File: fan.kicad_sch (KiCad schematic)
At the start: 16 parts, among them J10 Conn_01x04, J16 Conn_02x03_Counter_Clockwise, J2 Conn_01x02, J7 Conn_01x04, J8 Conn_01x02, J9 Conn_01x04, Q1 SS8050, U2 ICM-20948, U3 TXS0104EPW, U7 MAX98357A

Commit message: feat: semi-finalized PCB design
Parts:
- H1, H2, H3, H4: footprint MountingHole:MountingHole_2.2mm_M2 -> MountingHole:MountingHole_3.2mm_M3
- J16: footprint (none) -> Connector_PinHeader_2.54mm:PinHeader_2x03_P2.54mm_Vertical
- J8: footprint (none) -> Connector_PinHeader_2.54mm:PinHeader_1x02_P2.54mm_Vertical
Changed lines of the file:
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@@
 			)
 		)
-		(property "Footprint" ""
+		(property "Footprint" "Connector_PinHeader_2.54mm:PinHeader_2x03_P2.54mm_Vertical"
 			(at 101.6 175.26 0)
 			(effects
@@
 			)
 		)
-		(property "Footprint" "MountingHole:MountingHole_2.2mm_M2"
+		(property "Footprint" "MountingHole:MountingHole_3.2mm_M3"
 			(at 147.32 110.49 0)
 			(effects
@@
 			)
 		)
-		(property "Footprint" "MountingHole:MountingHole_2.2mm_M2"
+		(property "Footprint" "MountingHole:MountingHole_3.2mm_M3"
 			(at 147.32 115.57 0)
 			(effects
@@
 			)
 		)
-		(property "Footprint" ""
+		(property "Footprint" "Connector_PinHeader_2.54mm:PinHeader_1x02_P2.54mm_Vertical"
 			(at 86.36 153.67 0)
 			(effects
@@
 			)
 		)
-		(property "Footprint" "MountingHole:MountingHole_2.2mm_M2"
+		(property "Footprint" "MountingHole:MountingHole_3.2mm_M3"
 			(at 147.32 120.65 0)
 			(effects
@@
 			)
 		)
-		(property "Footprint" "MountingHole:MountingHole_2.2mm_M2"
+		(property "Footprint" "MountingHole:MountingHole_3.2mm_M3"
 			(at 147.32 125.73 0)
 			(effects

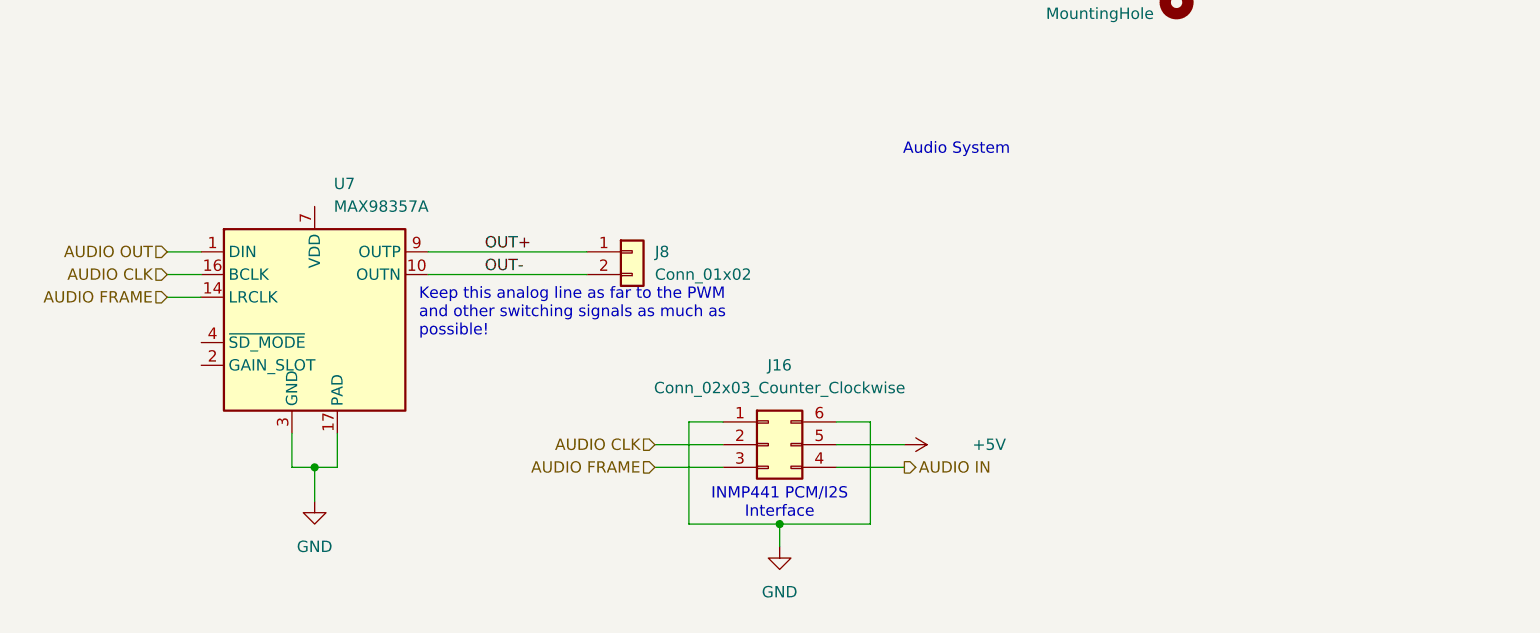
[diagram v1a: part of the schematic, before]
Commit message: feat: added optional right channel
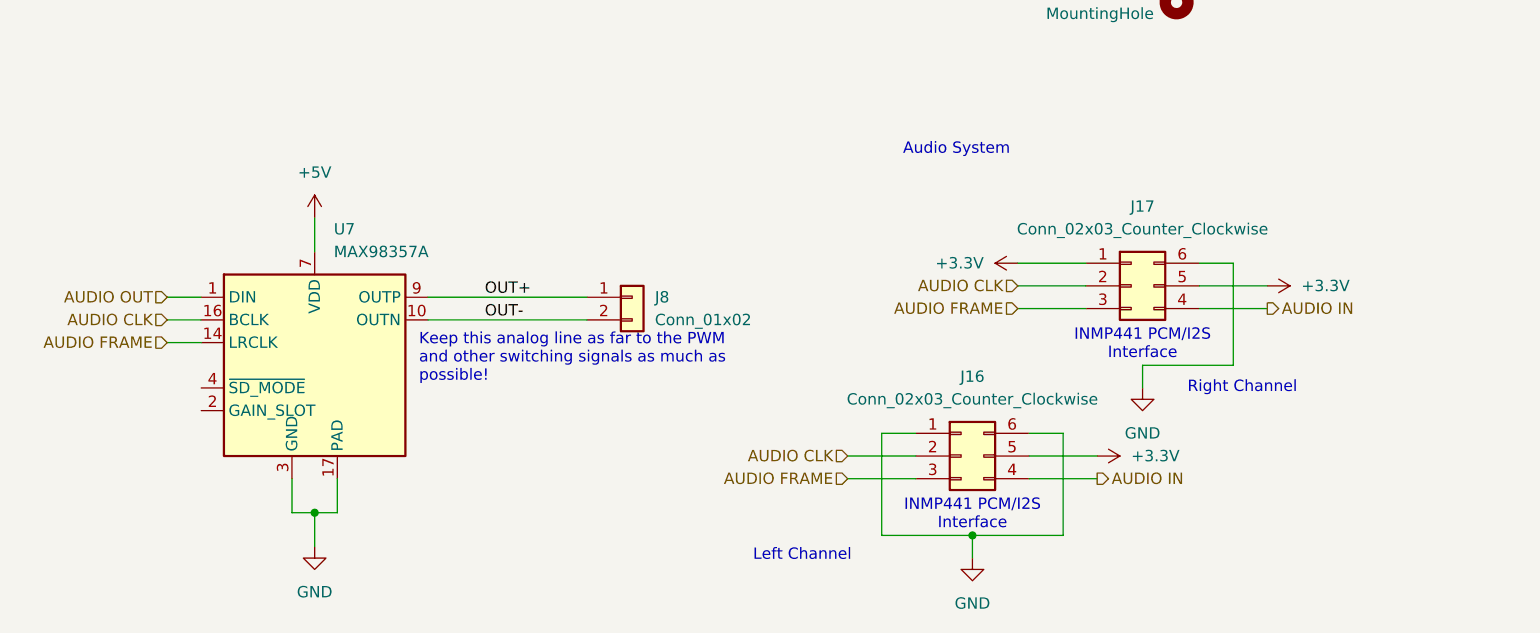
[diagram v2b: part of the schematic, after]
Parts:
- added J17: Conn_02x03_Counter_Clockwise, Connector_PinHeader_2.54mm:PinHeader_2x03_P2.54mm_Vertical, symbol Connector_Generic:Conn_02x03_Counter_Clockwise
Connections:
- net +3.3V: now also J16.5 (Pin_5), J17.1 (Pin_1), J17.5 (Pin_5)
- net +5V: now also U7.7 (VDD), U7.8 (VDD); no longer J16.5 (Pin_5)
- net AUDIO CLK: now also J17.2 (Pin_2)
- net AUDIO FRAME: now also J17.3 (Pin_3)
- net AUDIO IN: now also J17.4 (Pin_4)
- net GND: now also J17.6 (Pin_6)
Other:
- note added: "Left Channel"
- note added: "Right Channel"
- moved on the sheet: J16, J8, U7

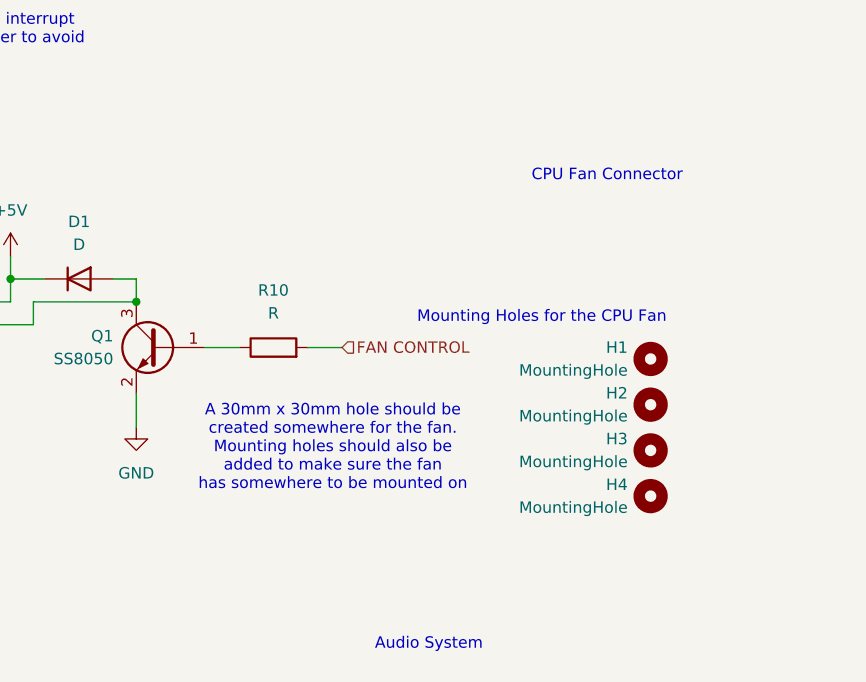
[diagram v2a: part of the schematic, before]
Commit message: feat: removed mounting holes for fan
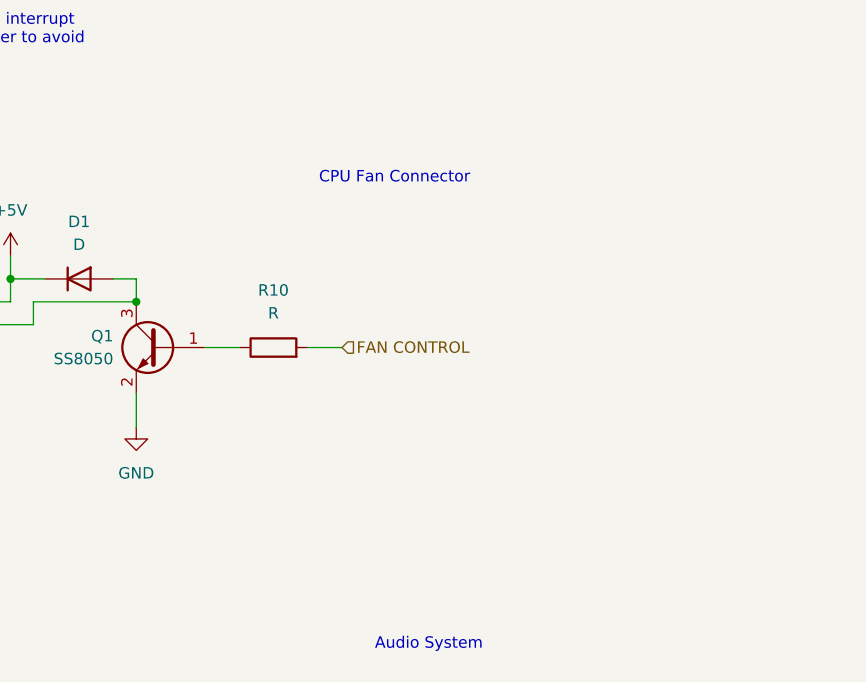
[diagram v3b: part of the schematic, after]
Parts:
- removed H1, H2, H3, H4: MountingHole, MountingHole:MountingHole_3.2mm_M3, symbol Mechanical:MountingHole
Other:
- note removed: "A 30mm x 30mm hole should be created somewhere for the fan. Mounting holes should also be added to make sure the fan has somewhere to be mounted on"
- note removed: "Mounting Holes for the CPU Fan"
